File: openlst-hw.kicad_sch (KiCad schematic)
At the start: 8 parts

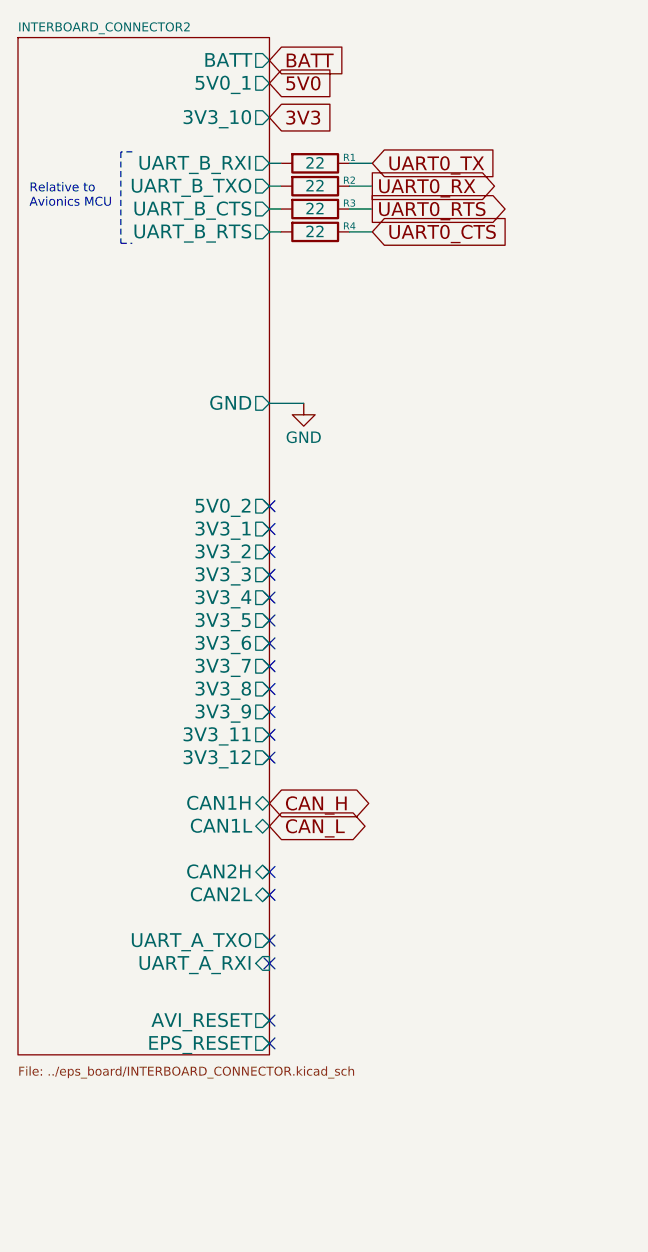
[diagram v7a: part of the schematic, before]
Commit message: flip can high low around to ease access from front side
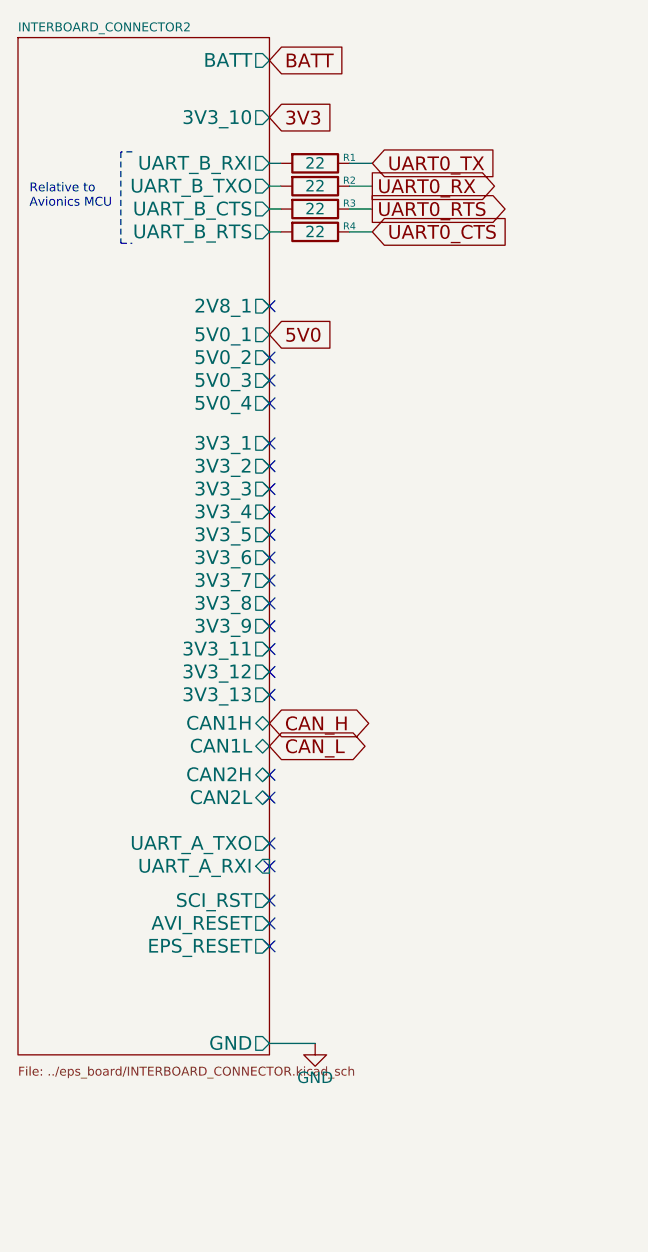
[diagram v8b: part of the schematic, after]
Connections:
- no-connect marks 18 -> 23
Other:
- sheet INTERBOARD_CONNECTOR2 ports: added 2V8_1, 3V3_13, 5V0_3, 5V0_4, SCI_RST; removed none
